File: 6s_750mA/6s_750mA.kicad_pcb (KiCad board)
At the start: 2 copper layers, 71.8 x 55.9 mm, 97 parts, among them J1 Barrel_Jack_MountingPin, J2 S6B-XH-A, U1 SN6505BDBV, U10 BQ25170DSGR, U11 SN6505BDBV, U12 BQ25170DSGR, U2 BQ25170DSGR, U3 SN6505BDBV, U4 BQ25170DSGR, U5 SN6505BDBV, U6 BQ25170DSGR, U7 SN6505BDBV, U8 BQ25170DSGR, U9 SN6505BDBV

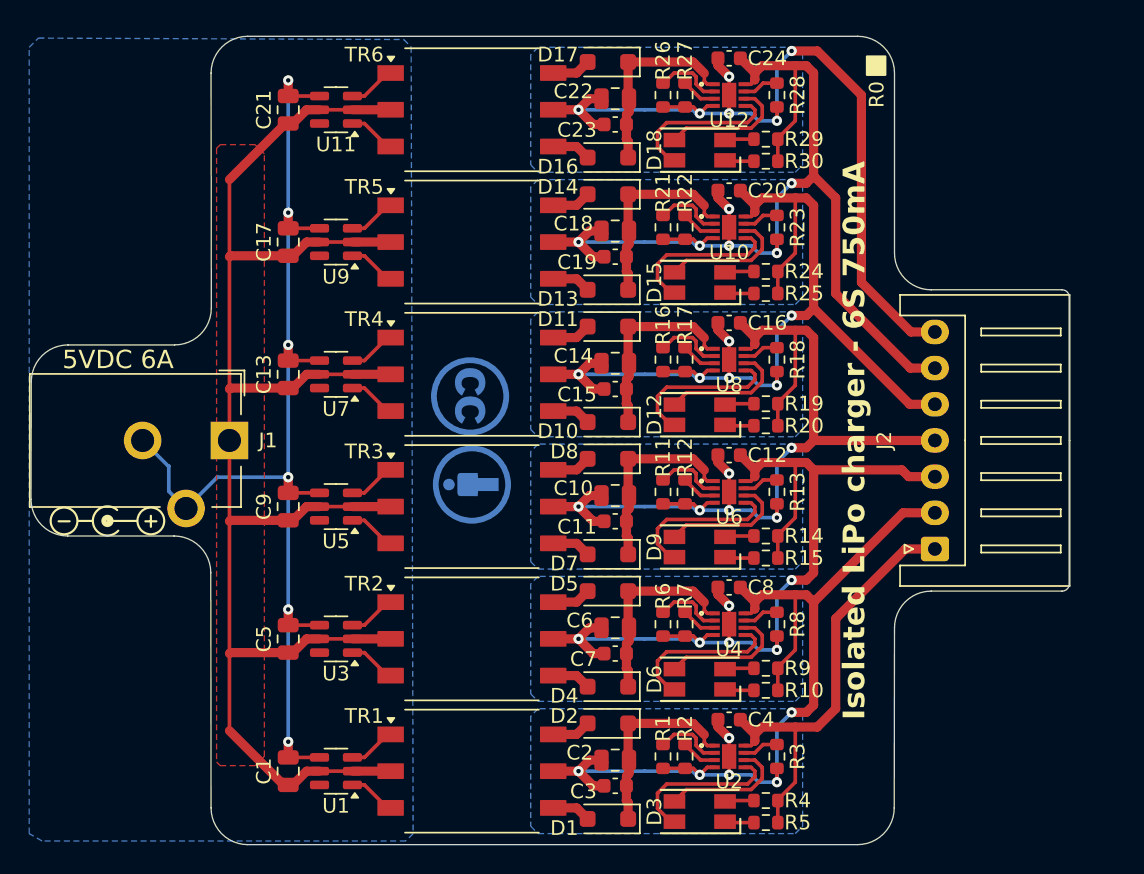
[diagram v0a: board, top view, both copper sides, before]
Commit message: update PCB with correct LED colors, and fix typo
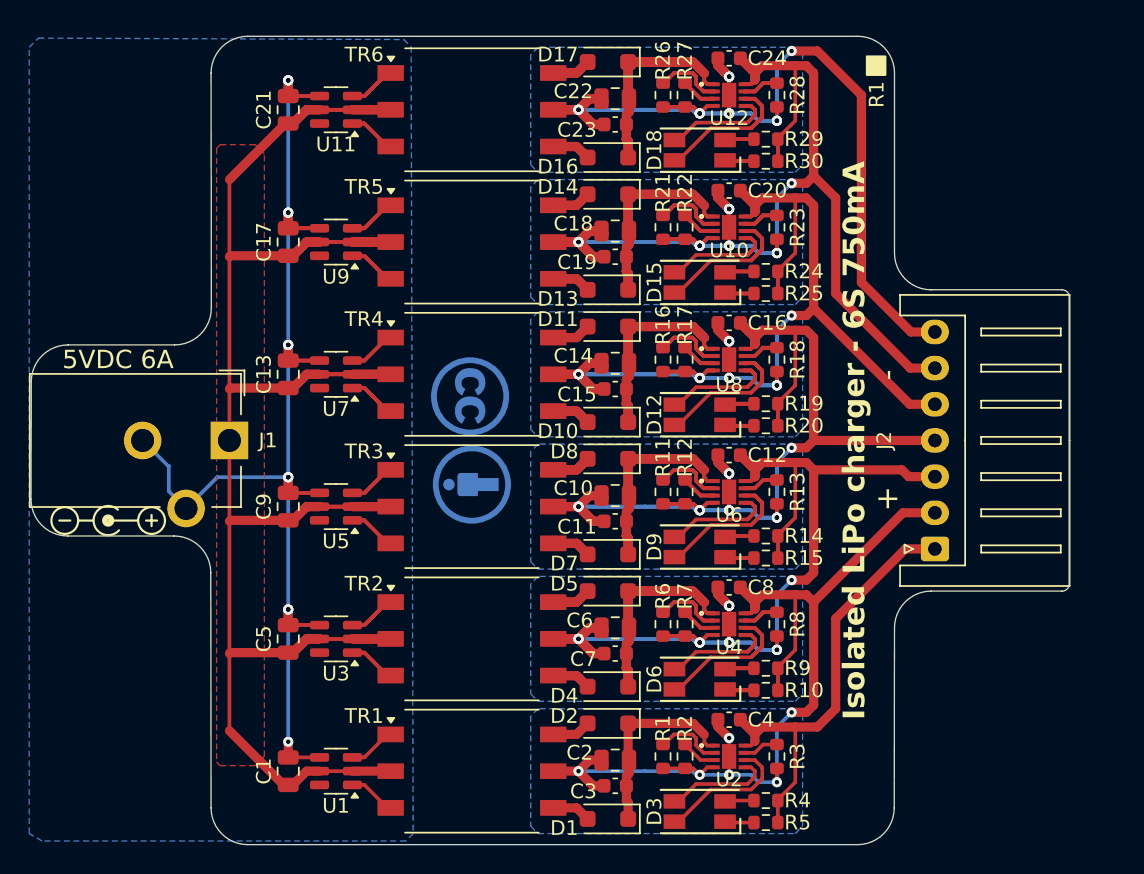
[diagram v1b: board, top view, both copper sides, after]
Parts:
- moved REF** 0.06 mm to (139.2, 92.8)
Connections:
- D12 pad 3: /charger3/PG -> /charger3/STAT
- D12 pad 4: /charger3/STAT -> /charger3/PG
- D15 pad 3: /charger4/PG -> /charger4/STAT
- D15 pad 4: /charger4/STAT -> /charger4/PG
- D18 pad 3: /charger5/PG -> /charger5/STAT
- D18 pad 4: /charger5/STAT -> /charger5/PG
- D3 pad 3: /charger0/PG -> /charger0/STAT
- D3 pad 4: /charger0/STAT -> /charger0/PG
- D6 pad 3: /charger1/PG -> /charger1/STAT
- D6 pad 4: /charger1/STAT -> /charger1/PG
- D9 pad 3: /charger2/PG -> /charger2/STAT
- D9 pad 4: /charger2/STAT -> /charger2/PG
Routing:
- net +5V: track 110.6 -> 149.6 mm
- net /charger4/Vo-: track 75.4 -> 113.5 mm, vias 6 -> 11
- net /charger3/Vo-: track 68.8 -> 106.9 mm, vias 6 -> 11
- net /charger1/Vo-: track 66.2 -> 104.3 mm, vias 6 -> 11
- net /charger2/Vo-: track 66.1 -> 104.1 mm, vias 6 -> 11
- net /charger5/Vo-: track 60.0 -> 93.0 mm, vias 6 -> 11
- net GND: track 79.2 -> 95.4 mm, vias 6 -> 11
- net Net-(D4-K): track 13.7 -> 27.4 mm
- net Net-(D13-K): track 13.7 -> 27.4 mm
- net Net-(D16-K): track 13.7 -> 27.4 mm
- net Net-(D7-K): track 13.7 -> 27.4 mm
- net Net-(D10-K): track 13.7 -> 27.4 mm
- net /charger0/Vo-: track 68.6 -> 73.7 mm
- net Net-(U12-ISET): track 4.68 -> 9.37 mm
- net Net-(U6-ISET): track 4.68 -> 9.37 mm
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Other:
- board text added: "+ -"
- board text added: "Isolated LiPo Charger 6S 750mA ©2024 by James Sarrett licensed under CC BY 4.0 github.com/jsarrett/StackedCharger"
- board text added: "R1"
- board text removed: "Isolated LiPo Charger 6S 750mA ©2024 by James Sarrett licensed under CC BY 4.0 github.com/jsarrett/StackedChargerr"
- board text removed: "R0"

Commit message: new layout using switching regulator
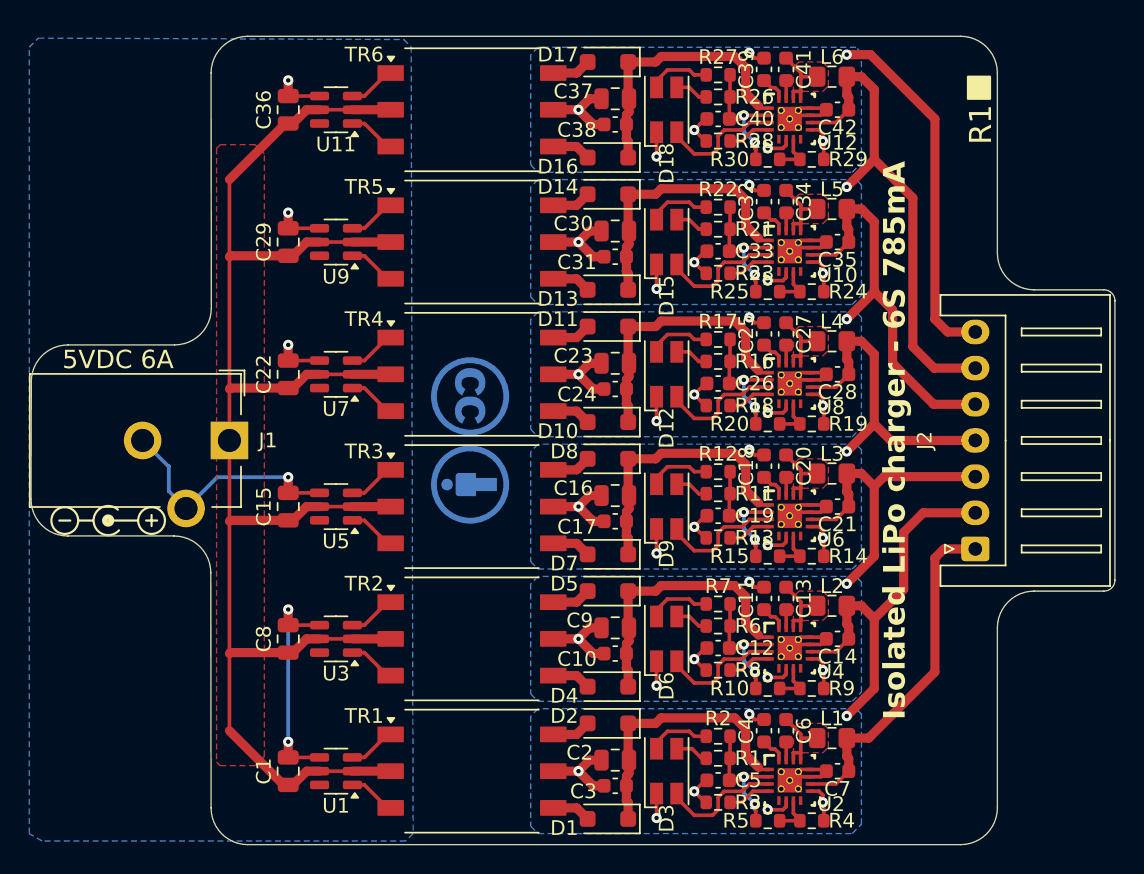
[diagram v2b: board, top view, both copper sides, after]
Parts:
- removed the R13 at (185.4, 90.9)
- removed the R18 at (185.4, 81.8)
- removed the R23 at (185.4, 72.6)
- removed the R28 at (185.4, 63.5)
- removed the R3 at (185.4, 109.2)
- removed the R8 at (185.4, 100.1)
- added C11: 10uF, Capacitor_SMD:C_0603_1608Metric, F.Cu at (184.5, 98.3)
- added C12: 2.2uF, Capacitor_SMD:C_0603_1608Metric, F.Cu at (181.4, 101.7)
- added C13: 47nF, Capacitor_SMD:C_0603_1608Metric, F.Cu at (186.1, 98.3)
- added C18: 10uF, Capacitor_SMD:C_0603_1608Metric, F.Cu at (184.5, 89.2)
- added C19: 2.2uF, Capacitor_SMD:C_0603_1608Metric, F.Cu at (181.4, 92.6)
- added C20: 47nF, Capacitor_SMD:C_0603_1608Metric, F.Cu at (186.1, 89.2)
- added C25: 10uF, Capacitor_SMD:C_0603_1608Metric, F.Cu at (184.5, 80.0)
- added C26: 2.2uF, Capacitor_SMD:C_0603_1608Metric, F.Cu at (181.4, 83.4)
- added C27: 47nF, Capacitor_SMD:C_0603_1608Metric, F.Cu at (186.1, 80.0)
- added C32: 10uF, Capacitor_SMD:C_0603_1608Metric, F.Cu at (184.5, 70.9)
- added C33: 2.2uF, Capacitor_SMD:C_0603_1608Metric, F.Cu at (181.4, 74.3)
- added C34: 47nF, Capacitor_SMD:C_0603_1608Metric, F.Cu at (186.1, 70.9)
- added C39: 10uF, Capacitor_SMD:C_0603_1608Metric, F.Cu at (184.5, 61.7)
- added C4: 10uF, Capacitor_SMD:C_0603_1608Metric, F.Cu at (184.5, 107.4)
- added C40: 2.2uF, Capacitor_SMD:C_0603_1608Metric, F.Cu at (181.4, 65.2)
- added C41: 47nF, Capacitor_SMD:C_0603_1608Metric, F.Cu at (186.1, 61.7)
- added C5: 2.2uF, Capacitor_SMD:C_0603_1608Metric, F.Cu at (181.4, 110.9)
- added C6: 47nF, Capacitor_SMD:C_0603_1608Metric, F.Cu at (186.1, 107.4)
- added L1: 4.7uH, Inductor_SMD:L_0805_2012Metric_Pad1.15x1.40mm_HandSolder, F.Cu at (189.2, 108.0)
- added L2: 4.7uH, Inductor_SMD:L_0805_2012Metric_Pad1.15x1.40mm_HandSolder, F.Cu at (189.2, 98.8)
- added L3: 4.7uH, Inductor_SMD:L_0805_2012Metric_Pad1.15x1.40mm_HandSolder, F.Cu at (189.2, 89.7)
- added L4: 4.7uH, Inductor_SMD:L_0805_2012Metric_Pad1.15x1.40mm_HandSolder, F.Cu at (189.2, 80.5)
- added L5: 4.7uH, Inductor_SMD:L_0805_2012Metric_Pad1.15x1.40mm_HandSolder, F.Cu at (189.2, 71.4)
- added L6: 4.7uH, Inductor_SMD:L_0805_2012Metric_Pad1.15x1.40mm_HandSolder, F.Cu at (189.2, 62.2)
- added R10: 10k, Resistor_SMD:R_0603_1608Metric, F.Cu at (184.8, 104.5)
- added R15: 10k, Resistor_SMD:R_0603_1608Metric, F.Cu at (184.8, 95.4)
- added R20: 10k, Resistor_SMD:R_0603_1608Metric, F.Cu at (184.8, 86.2)
- added R25: 10k, Resistor_SMD:R_0603_1608Metric, F.Cu at (184.8, 77.1)
- added R30: 10k, Resistor_SMD:R_0603_1608Metric, F.Cu at (184.8, 67.9)
- added R5: 10k, Resistor_SMD:R_0603_1608Metric, F.Cu at (184.8, 113.7)
- C14: renamed from C8; value 1uF -> 10uF
- C21: renamed from C12; value 1uF -> 10uF
- C28: renamed from C16; value 1uF -> 10uF
- C35: renamed from C20; value 1uF -> 10uF
- C42: renamed from C24; value 1uF -> 10uF
- C7: renamed from C4; value 1uF -> 10uF
- D12, D15, D18, D3, D6, D9: footprint LED_SMD:LED_RGB_1210 -> LED_SMD:LED_RGB_Wuerth-PLCC4_3.2x2.8mm_150141M173100
- R13: renamed from R11; value 390 -> 51k
- R18: renamed from R16; value 390 -> 51k
- R23: renamed from R21; value 390 -> 51k
- R28: renamed from R26; value 390 -> 51k
- R3: renamed from R1; value 390 -> 51k
- R8: renamed from R6; value 390 -> 51k
- U10, U12, U2, U4, U6, U8: value BQ25170DSGR -> BQ25302RTER; footprint StackedCharger:WSON8_BQ2517_TEX -> StackedCharger:RTE0016C
- moved R19 9.83 mm to (187.8, 86.2), turned to 0 degrees
- moved R4 9.83 mm to (187.8, 113.7), turned to 0 degrees
- moved R9 9.83 mm to (187.8, 104.5), turned to 0 degrees
- moved R14 9.83 mm to (187.8, 95.4), turned to 0 degrees
- moved R24 9.83 mm to (187.8, 77.1), turned to 0 degrees
- moved R29 9.83 mm to (187.8, 67.9), turned to 0 degrees
- moved C42 8.29 mm to (189.6, 64.5)
- moved C14 8.29 mm to (189.6, 101.1)
- moved C21 8.29 mm to (189.6, 91.9)
- moved C28 8.29 mm to (189.6, 82.8)
- moved C35 8.29 mm to (189.6, 73.7)
- moved C7 8.29 mm to (189.6, 110.2)
- moved R12 6.82 mm to (181.4, 89.5)
- moved R2 6.82 mm to (181.4, 107.8)
- moved R27 6.82 mm to (181.4, 62.1)
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- renumbered C7 to C10, C9 to C15, C10 to C16, C11 to C17, C13 to C22, C14 to C23, C15 to C24, C17 to C29, C18 to C30, C19 to C31, C21 to C36, C22 to C37, C23 to C38, C5 to C8, C6 to C9, R4 to R1, R14 to R11, R15 to R12, R12 to R14, R19 to R16, R20 to R17, R17 to R19, R5 to R2, R24 to R21, R25 to R22, R22 to R24, R29 to R26, R30 to R27, R27 to R29, R2 to R4, R9 to R6, R10 to R7, R7 to R9
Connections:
- net Net-(D1-K) renamed /charger0/V_iso
- net Net-(D10-K) renamed /charger3/V_iso
- net Net-(D13-K) renamed /charger4/V_iso
- net Net-(D16-K) renamed /charger5/V_iso
- net Net-(D4-K) renamed /charger1/V_iso
- net Net-(D7-K) renamed /charger2/V_iso
- D12 pad 3: /charger3/STAT -> /charger3/Vo-
- D12 pad 4: /charger3/PG -> /charger3/STAT
- D15 pad 3: /charger4/STAT -> /charger4/Vo-
- D15 pad 4: /charger4/PG -> /charger4/STAT
- D18 pad 3: /charger5/STAT -> /charger5/Vo-
- D18 pad 4: /charger5/PG -> /charger5/STAT
- D3 pad 3: /charger0/STAT -> /charger0/Vo-
- D3 pad 4: /charger0/PG -> /charger0/STAT
- D6 pad 3: /charger1/STAT -> /charger1/Vo-
- D6 pad 4: /charger1/PG -> /charger1/STAT
- D9 pad 3: /charger2/STAT -> /charger2/Vo-
- D9 pad 4: /charger2/PG -> /charger2/STAT
- R1 pad 1: /charger0/Vo+ -> /charger0/REGN
- R11 pad 1: /charger1/Vo- -> /charger2/REGN
- R12 pad 1: /charger1/Vo- -> /charger2/REGN
- R13 pad 1: Net-(U6-ISET) -> Net-(U6-ICHG)
- R16 pad 1: /charger2/Vo- -> /charger3/REGN
- R17 pad 1: /charger2/Vo- -> /charger3/REGN
- R18 pad 1: Net-(U8-ISET) -> Net-(U8-ICHG)
- R2 pad 1: /charger0/Vo+ -> /charger0/REGN
- R21 pad 1: /charger3/Vo- -> /charger4/REGN
- R22 pad 1: /charger3/Vo- -> /charger4/REGN
- R23 pad 1: Net-(U10-ISET) -> Net-(U10-ICHG)
- R26 pad 1: /charger4/Vo- -> /charger5/REGN
- R27 pad 1: /charger4/Vo- -> /charger5/REGN
- R28 pad 1: Net-(U12-ISET) -> Net-(U12-ICHG)
- R3 pad 1: Net-(U2-ISET) -> Net-(U2-ICHG)
- R6 pad 1: /charger0/Vo- -> /charger1/REGN
- R7 pad 1: /charger0/Vo- -> /charger1/REGN
- R8 pad 1: Net-(U4-ISET) -> Net-(U4-ICHG)
- U10 pad 2: Net-(U10-ISET) -> /charger4/REGN
- U10 pad 3: Net-(U10-TS) -> /charger4/STAT
- U10 pad 4: /charger4/Vo- -> Net-(U10-ICHG)
- U10 pad 5: /charger4/STAT -> unconnected-(U10-NC(POL)-Pad5)
- U10 pad 6: /charger4/PG -> /charger4/Vo-
- U10 pad 7: Net-(U10-VSET) -> Net-(U10-TS)
- U10 pad 8: /charger3/Vo- -> unconnected-(U10-NC-Pad8)
- U12 pad 2: Net-(U12-ISET) -> /charger5/REGN
- U12 pad 3: Net-(U12-TS) -> /charger5/STAT
- U12 pad 4: /charger5/Vo- -> Net-(U12-ICHG)
- U12 pad 5: /charger5/STAT -> unconnected-(U12-NC(POL)-Pad5)
- U12 pad 6: /charger5/PG -> /charger5/Vo-
- U12 pad 7: Net-(U12-VSET) -> Net-(U12-TS)
- U12 pad 8: /charger4/Vo- -> unconnected-(U12-NC-Pad8)
- U2 pad 2: Net-(U2-ISET) -> /charger0/REGN
- U2 pad 3: Net-(U2-TS) -> /charger0/STAT
- U2 pad 4: /charger0/Vo- -> Net-(U2-ICHG)
- U2 pad 5: /charger0/STAT -> unconnected-(U2-NC(POL)-Pad5)
- U2 pad 6: /charger0/PG -> /charger0/Vo-
- U2 pad 7: Net-(U2-VSET) -> Net-(U2-TS)
- U2 pad 8: /charger0/Vo+ -> unconnected-(U2-NC-Pad8)
- U4 pad 2: Net-(U4-ISET) -> /charger1/REGN
- U4 pad 3: Net-(U4-TS) -> /charger1/STAT
- U4 pad 4: /charger1/Vo- -> Net-(U4-ICHG)
- U4 pad 5: /charger1/STAT -> unconnected-(U4-NC(POL)-Pad5)
- U4 pad 6: /charger1/PG -> /charger1/Vo-
- U4 pad 7: Net-(U4-VSET) -> Net-(U4-TS)
- U4 pad 8: /charger0/Vo- -> unconnected-(U4-NC-Pad8)
- U6 pad 2: Net-(U6-ISET) -> /charger2/REGN
- U6 pad 3: Net-(U6-TS) -> /charger2/STAT
- U6 pad 4: /charger2/Vo- -> Net-(U6-ICHG)
- U6 pad 5: /charger2/STAT -> unconnected-(U6-NC(POL)-Pad5)
- U6 pad 6: /charger2/PG -> /charger2/Vo-
- U6 pad 7: Net-(U6-VSET) -> Net-(U6-TS)
- U6 pad 8: /charger1/Vo- -> unconnected-(U6-NC-Pad8)
- U8 pad 2: Net-(U8-ISET) -> /charger3/REGN
- U8 pad 3: Net-(U8-TS) -> /charger3/STAT
- U8 pad 4: /charger3/Vo- -> Net-(U8-ICHG)
- U8 pad 5: /charger3/STAT -> unconnected-(U8-NC(POL)-Pad5)
- U8 pad 6: /charger3/PG -> /charger3/Vo-
- U8 pad 7: Net-(U8-VSET) -> Net-(U8-TS)
- U8 pad 8: /charger2/Vo- -> unconnected-(U8-NC-Pad8)
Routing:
- net /charger1/Vo-: track 104.3 -> 42.9 mm, vias 11 -> 7
- net /charger2/Vo-: track 104.1 -> 43.1 mm, vias 11 -> 7
- net /charger3/Vo-: track 106.9 -> 48.0 mm, vias 11 -> 7
- net /charger4/Vo-: track 113.5 -> 54.6 mm, vias 11 -> 7
- net GND: track 95.4 -> 42.6 mm, vias 11 -> 6
- net /charger5/Vo-: track 93.0 -> 45.4 mm, vias 11 -> 7
- net +5V: track 149.6 -> 112.0 mm
- net /charger0/Vo-: track 73.7 -> 47.9 mm, vias 6 -> 7
- net /charger3/PG: track 12.9 -> 0.00 mm
- net /charger5/PG: track 12.9 -> 0.00 mm
- net /charger4/PG: track 12.9 -> 0.00 mm
- net /charger2/PG: track 12.9 -> 0.00 mm
- net /charger1/PG: track 12.9 -> 0.00 mm
- net /charger0/PG: track 9.56 -> 0.00 mm
- net Net-(U12-ISET): track 9.37 -> 0.00 mm
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- added copper zone on F.Cu, net /charger0/V_sw
- added copper zone on F.Cu, net /charger1/V_sw
- added copper zone on F.Cu, net /charger2/V_sw
- added copper zone on F.Cu, net /charger3/V_sw
- added copper zone on F.Cu, net /charger4/V_sw
- added copper zone on F.Cu, net /charger5/V_sw
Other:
- board size 71.8 x 55.9 mm -> 74.9 x 55.9 mm
- board text added: "Isolated LiPo charger - 6S 785mA"
- board text added: "locked"
- board text removed: "+ -"
- board text removed: "Isolated LiPo Charger 6S 750mA ©2024 by James Sarrett licensed under CC BY 4.0 github.com/jsarrett/StackedCharger"
- board text removed: "Isolated LiPo charger - 6S 750mA"
